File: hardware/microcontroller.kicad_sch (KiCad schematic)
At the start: 19 parts, among them J5 1x2 jumper right-angle, J6 Conn_02x03_Odd_Even, J7 1x2 jumper right-angle, U15 74LVC138, U16 74LV1T125, U17 74LVC138

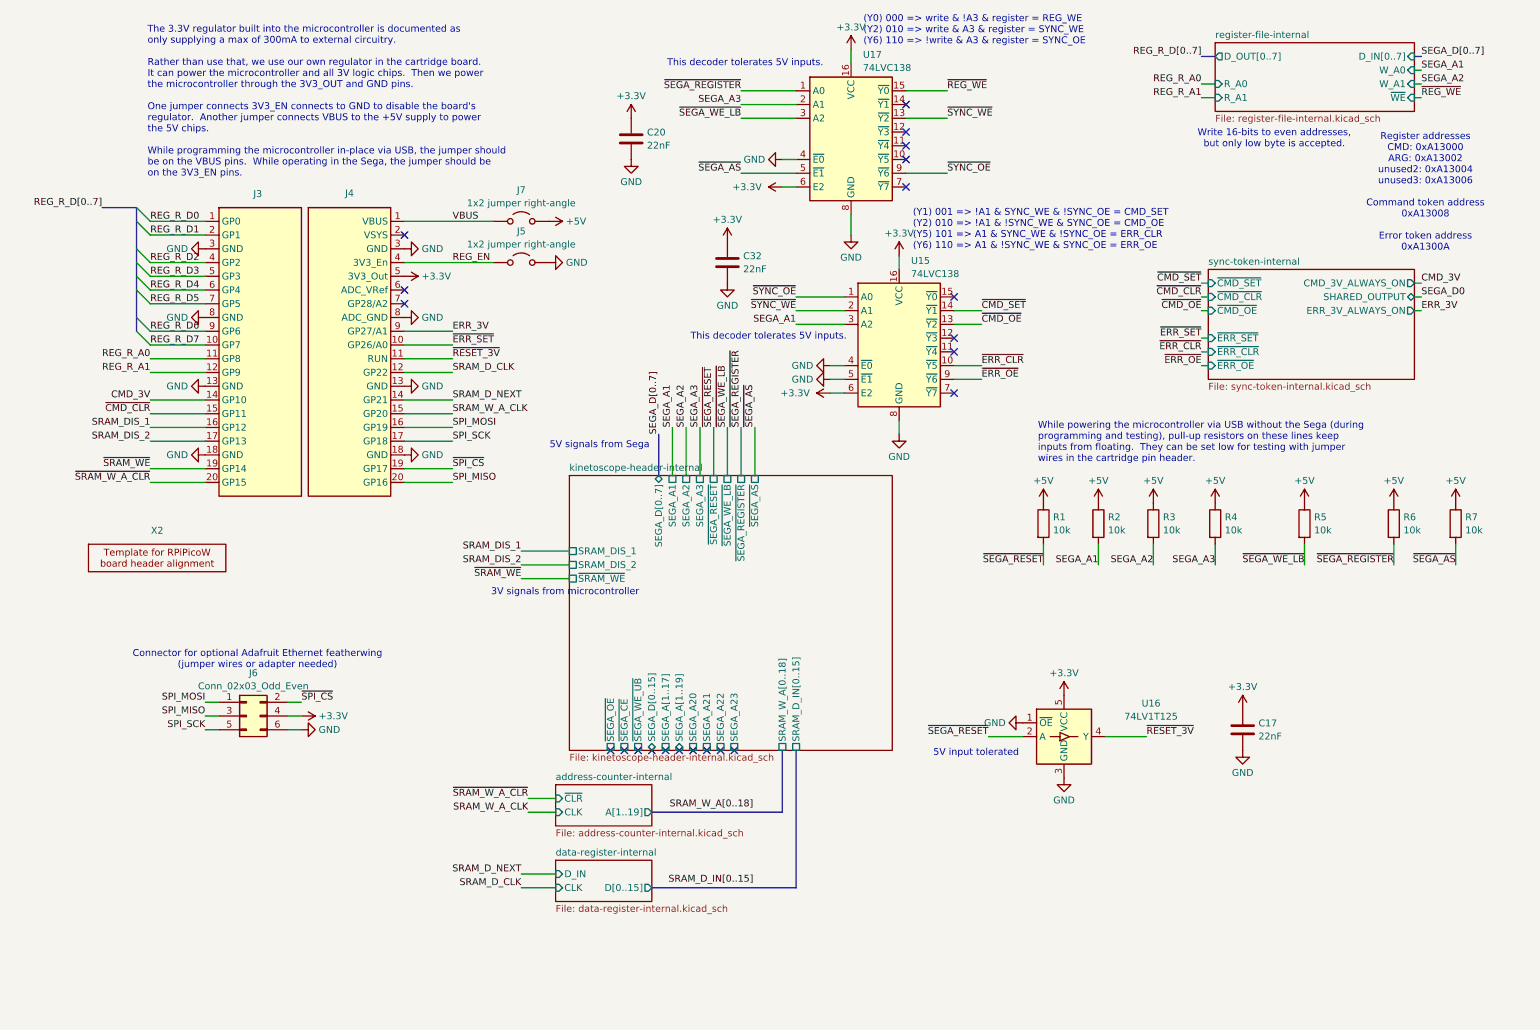
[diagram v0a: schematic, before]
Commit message: Fix microcontroller address decoders
Verified on a breadboard
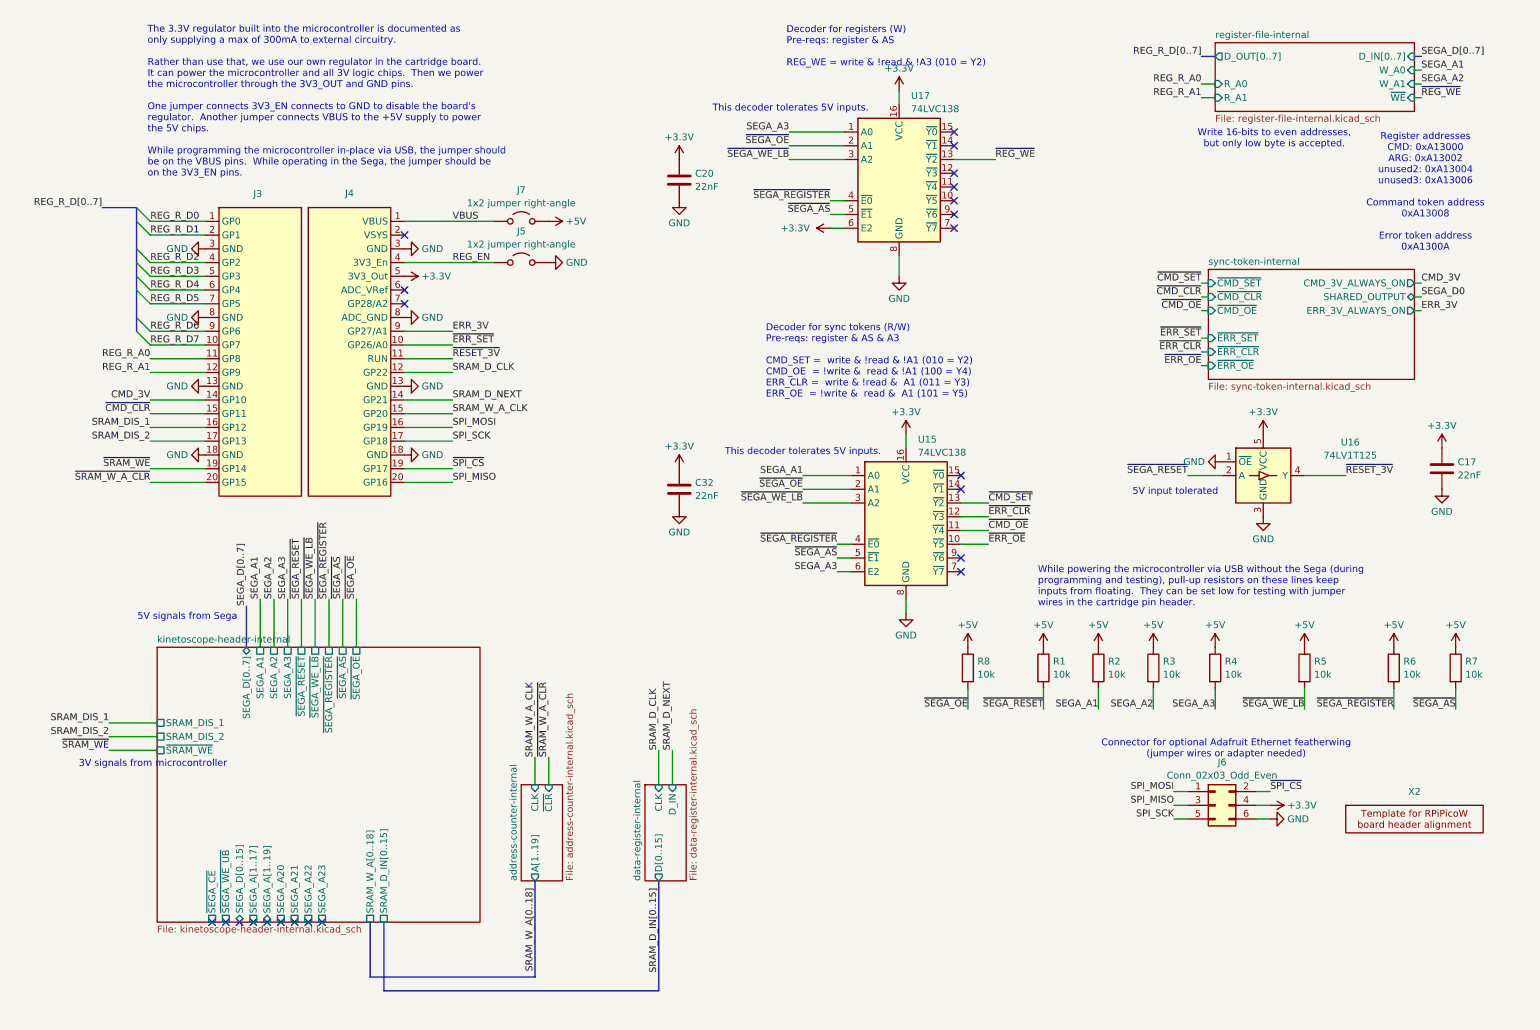
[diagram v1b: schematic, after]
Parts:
- added R8: 10k, Resistor_SMD:R_0603_1608Metric, symbol Device:R
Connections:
- net +3.3V: no longer U15.6 (E2)
- net +5V: now also R8.1
- net GND: no longer U15.4 (~{E0}), U15.5 (~{E1}), U17.4 (~{E0})
- net SEGA_A1: now also U15.1 (A0); no longer U15.3 (A2)
- net SEGA_A3: now also U15.6 (E2), U17.1 (A0); no longer U17.2 (A1)
- net ~{CMD_OE}: now also U15.11 (~{Y4}); no longer U15.13 (~{Y2})
- net ~{CMD_SET}: now also U15.13 (~{Y2}); no longer U15.14 (~{Y1})
- net ~{ERR_CLR}: now also U15.12 (~{Y3}); no longer U15.10 (~{Y5})
- net ~{ERR_OE}: now also U15.10 (~{Y5}); no longer U15.9 (~{Y6})
- net ~{REG_WE}: now also U17.13 (~{Y2}); no longer U17.15 (~{Y0})
- net ~{SEGA_AS}: now also U15.5 (~{E1})
- net ~{SEGA_REGISTER}: now also U15.4 (~{E0}), U17.4 (~{E0}); no longer U17.1 (A0)
- net ~{SEGA_WE_LB}: now also U15.3 (A2)
- net ~{SYNC_OE}: no longer names the net of U17.9 (~{Y6})
- net ~{SYNC_OE}: no longer U15.1 (A0)
- net ~{SYNC_WE} renamed ~{SEGA_OE}
- net ~{SEGA_OE}: now also U17.2 (A1), R8.2; no longer U17.13 (~{Y2})
- no-connect marks 22 -> 23
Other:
- note added: "Decoder for registers (W) Pre-reqs: register & AS REG_WE = write & !read & !A3 (010 = Y2)"
- note added: "Decoder for sync tokens (R/W) Pre-reqs: register & AS & A3 CMD_SET = write & !read & !A1 (010 = Y2) CMD_OE = !write & read & !A1 (100 = Y4) ERR_CLR = write & !read & A1 (011 = Y3) ERR_OE = !write & read & A1 (101 = Y5)"
- note removed: "(Y0) 000 => write & !A3 & register = REG_WE (Y2) 010 => write & A3 & register = SYNC_WE (Y6) 110 => !write & A3 & register = SYNC_OE"
- note removed: "(Y1) 001 => !A1 & SYNC_WE & !SYNC_OE = CMD_SET (Y2) 010 => !A1 & !SYNC_WE & SYNC_OE = CMD_OE (Y5) 101 => A1 & SYNC_WE & !SYNC_OE = ERR_CLR (Y6) 110 => A1 & !SYNC_WE & SYNC_OE = ERR_OE"
- moved on the sheet: C17, C20, C32, J6, R1, R2, R3, R4, R5, R6, R7, U15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

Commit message: Simplify microcontroller board BOM
Replace 74LV1T125 with 74LVC2G125, which simplifies the BOM by removing one special part.
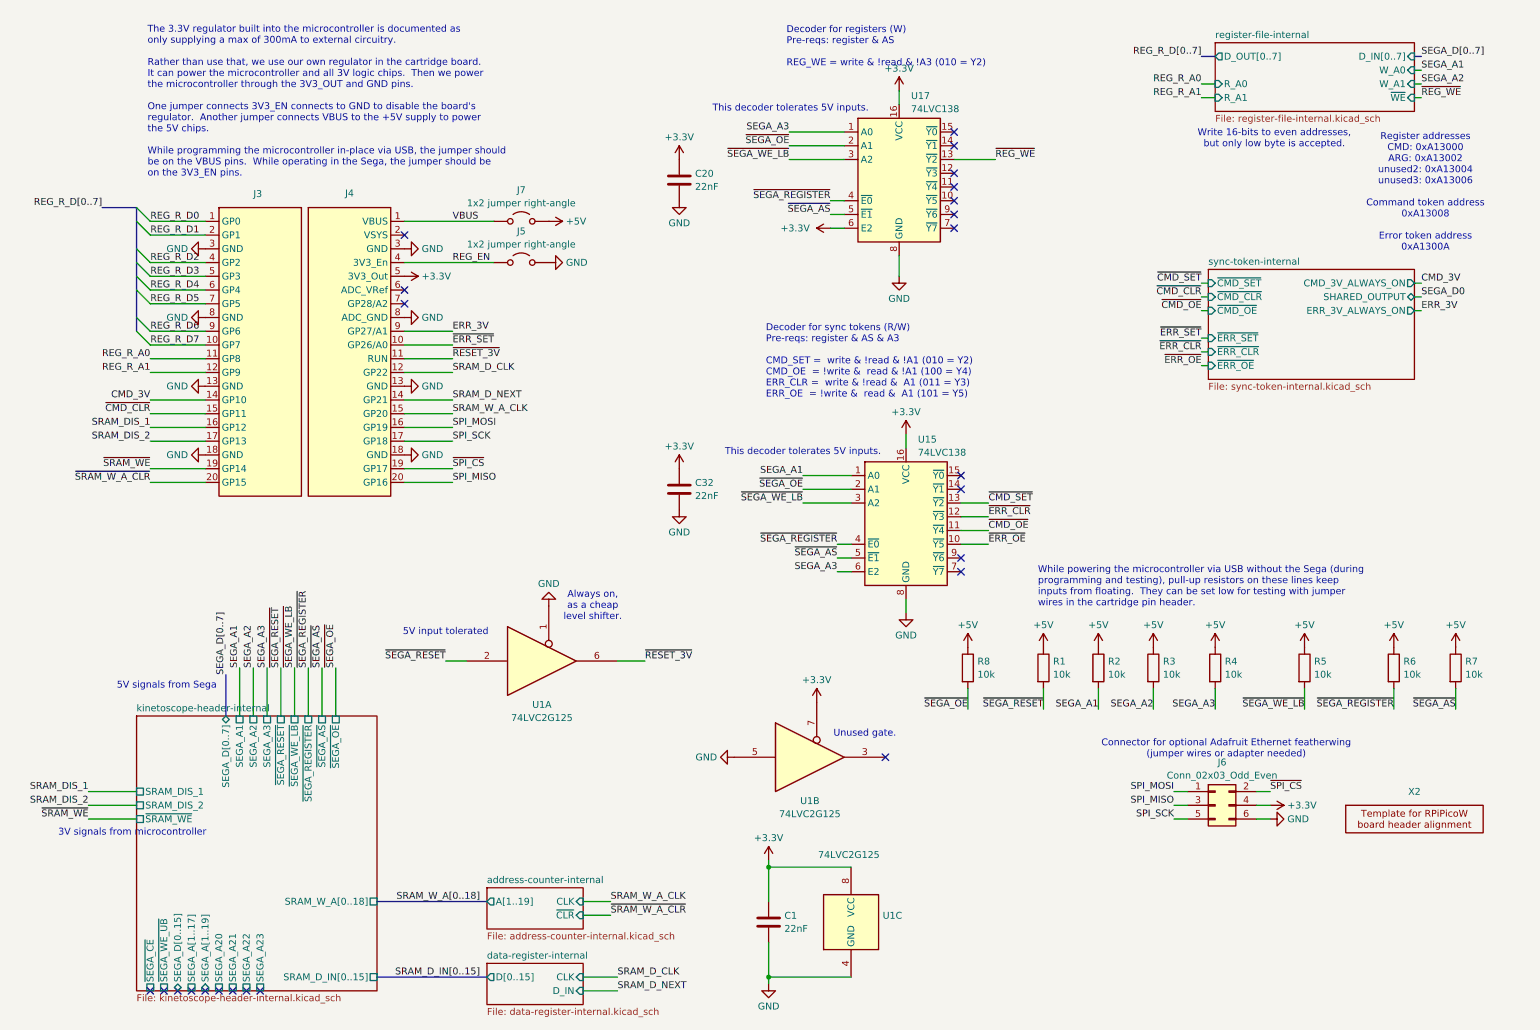
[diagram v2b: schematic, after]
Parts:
- removed C17: 22nF, Capacitor_SMD:C_0603_1608Metric, symbol Device:C
- removed U16: 74LV1T125, Package_TO_SOT_SMD:SOT-23-5, symbol Logic_LevelTranslator:SN74LV1T125DBV
- added C1: 22nF, Capacitor_SMD:C_0603_1608Metric, symbol Device:C
- added U1: 74LVC2G125, Package_SO:VSSOP-8_2.3x2mm_P0.5mm, symbol 74xGxx:74LVC2G125
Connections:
- net +3.3V: now also C1.1, U1.7, U1.8 (VCC)
- net GND: now also C1.2, U1.1, U1.4 (GND), U1.5
- net ~{RESET_3V}: now also U1.6
- net ~{SEGA_RESET}: now also U1.2
- no-connect marks 23 -> 24
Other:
- note added: "Always on, as a cheap level shifter."
- note added: "Unused gate."

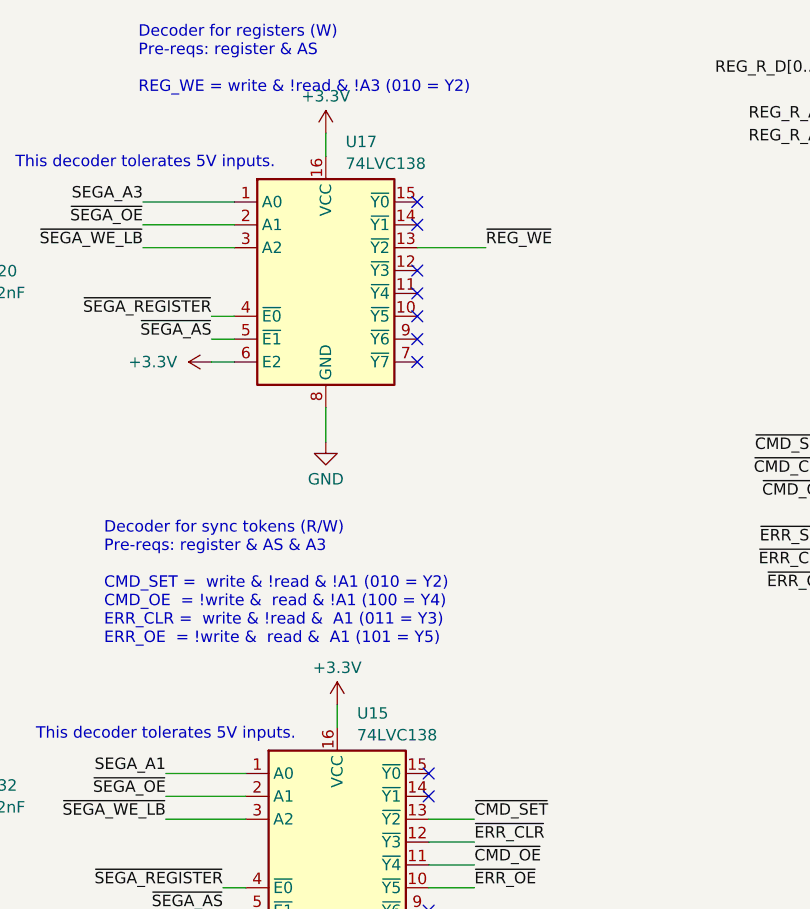
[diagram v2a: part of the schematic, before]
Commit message: Tweak part numbers
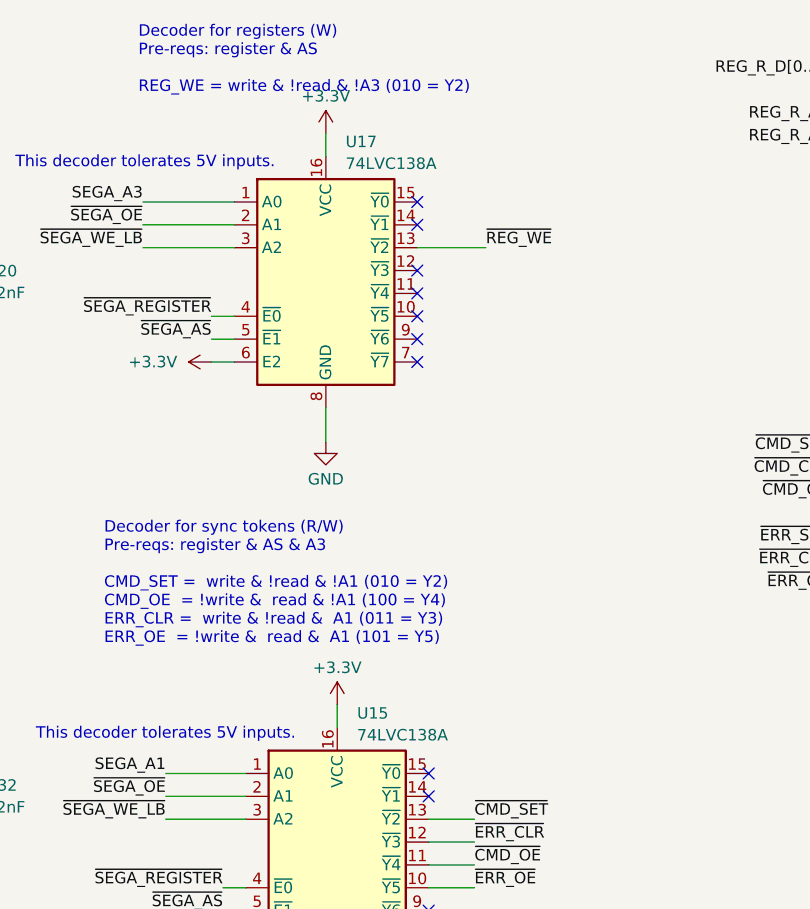
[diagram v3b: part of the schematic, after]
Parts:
- U15, U17: value 74LVC138 -> 74LVC138A
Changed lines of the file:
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@@
 			)
 		)
-		(property "Value" "74LVC138"
+		(property "Value" "74LVC138A"
 			(at 176.1841 30.0298 0)
 			(effects
@@
 			)
 		)
-		(property "Value" "74LVC138"
+		(property "Value" "74LVC138A"
 			(at 177.4541 93.5298 0)
 			(effects
